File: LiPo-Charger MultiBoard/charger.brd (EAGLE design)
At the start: 50 x 50 mm, 25 parts, among them IC1 MCP73832T, IC2 MCP73832T

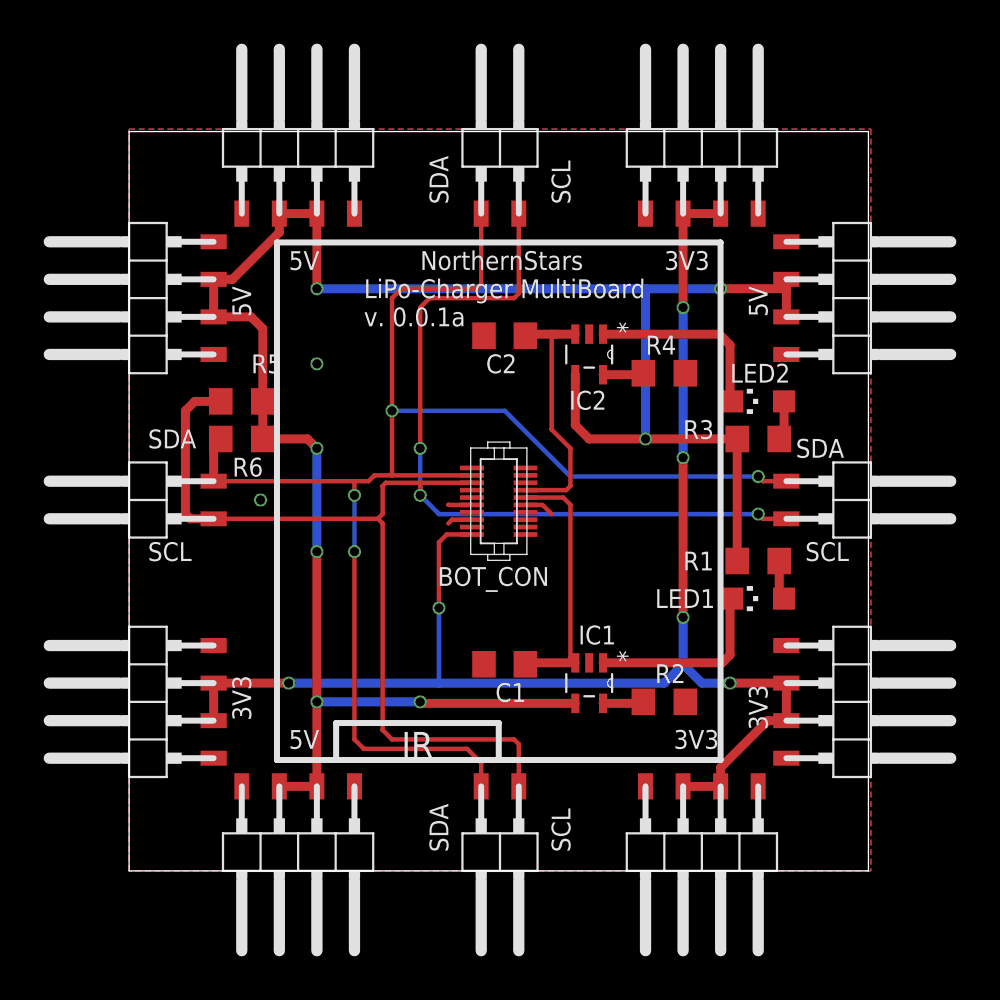
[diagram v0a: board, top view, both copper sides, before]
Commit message: Updated schematics and board. Added LibreOffice calculation for part lists.
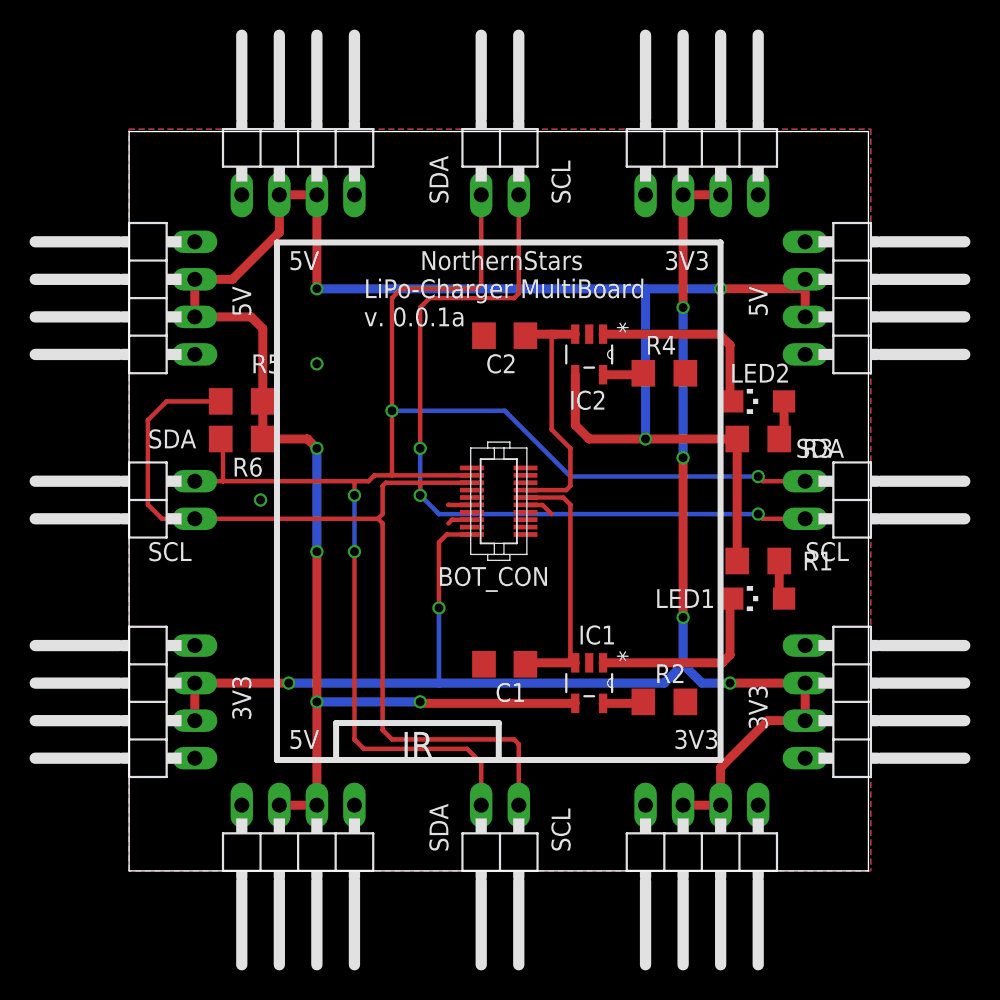
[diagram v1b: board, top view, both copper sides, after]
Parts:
- FEMALE_B, FEMALE_R, MALE_L, MALE_T: device pinhead-2:1X02SMD/90 -> pinhead-2:1X02/90
- FEMALE_BL, FEMALE_BR, FEMALE_RB, FEMALE_RT, MALE_LB, MALE_LT, MALE_TL, MALE_TR: device pinhead-2:1X04SMD/90 -> pinhead-2:1X04/90
- R1, R3: value 130R -> 470R
- R2, R4: value 2k -> 5k6
- moved FEMALE_BL 2.54 mm to (11.4, 0.64)
- moved FEMALE_RB 2.54 mm to (49.5, 11.4)
- moved FEMALE_BR 2.54 mm to (38.7, 0.64)
- moved FEMALE_RT 2.54 mm to (49.5, 38.7)
- moved MALE_LB 2.54 mm to (0.64, 11.4)
- moved MALE_LT 2.54 mm to (0.64, 38.7)
- moved MALE_TL 2.54 mm to (11.4, 49.5)
- moved MALE_TR 2.54 mm to (38.7, 49.5)
- moved FEMALE_B 1.27 mm to (23.8, 0.64)
- moved FEMALE_R 1.27 mm to (49.5, 23.8)
- moved MALE_L 1.27 mm to (0.64, 26.4)
- moved MALE_T 1.27 mm to (26.4, 49.5)
- turned R1 to 180 degrees
- turned R3 to 180 degrees
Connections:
- net +5V: now also R1.2, R3.2; no longer R1.1, R3.1
- net N$2: now also R1.1; no longer R1.2
- net N$5: now also R3.1; no longer R3.2
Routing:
- net SCL: track 109.6 -> 117.7 mm
- net +5V: track 142.6 -> 150.2 mm
- net +3V3: track 99.4 -> 104.5 mm
- net SDA: track 100.8 -> 105.8 mm
